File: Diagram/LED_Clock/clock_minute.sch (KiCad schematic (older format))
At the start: 34 parts, among them U3 MCP23017-E_SP

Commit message: updated
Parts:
- U3: symbol LED_Clock-rescue:MCP23017-E_SP-dk_Interface-I-O-Expanders -> Personal:MCP23017-Min
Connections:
- net at R8.2: now also U3.23 (GPA2); no longer U3.22 (GPA1)
- net at R9.2: now also U3.22 (GPA1); no longer U3.23 (GPA2)
- net at R14.2: now also U3.4 (GPB3); no longer U3.28 (GPA7)
- net at U3.21 (GPA0): now also R10.2; no longer R7.2
- net at U3.24 (GPA3): now also R7.2; no longer R10.2
- net at U3.25 (GPA4): now also R21.2; no longer R11.2
- net at U3.26 (GPA5): now also R20.2; no longer R12.2
- net at U3.27 (GPA6): now also R19.2; no longer R13.2
- net GPB0: no longer names the net of U3.1 (GPB0)
- net GPB0: now also R17.2; no longer R15.2
- net GPB1: no longer names the net of R16.2, U3.2 (GPB1)
- net GPB2: no longer names the net of U3.3 (GPB2)
- net GPB2: now also R15.2; no longer R17.2
- net GPB3: no longer names the net of R18.2
- net GPB3: now also U3.28 (GPA7); no longer U3.4 (GPB3)
- net GPB4: no longer names the net of U3.5 (GPB4)
- net GPB4: now also R13.2; no longer R19.2
- net GPB5: no longer names the net of U3.6 (GPB5)
- net GPB5: now also R12.2; no longer R20.2
- net GPB6: no longer names the net of U3.7 (GPB6)
- net GPB6: now also R11.2; no longer R21.2

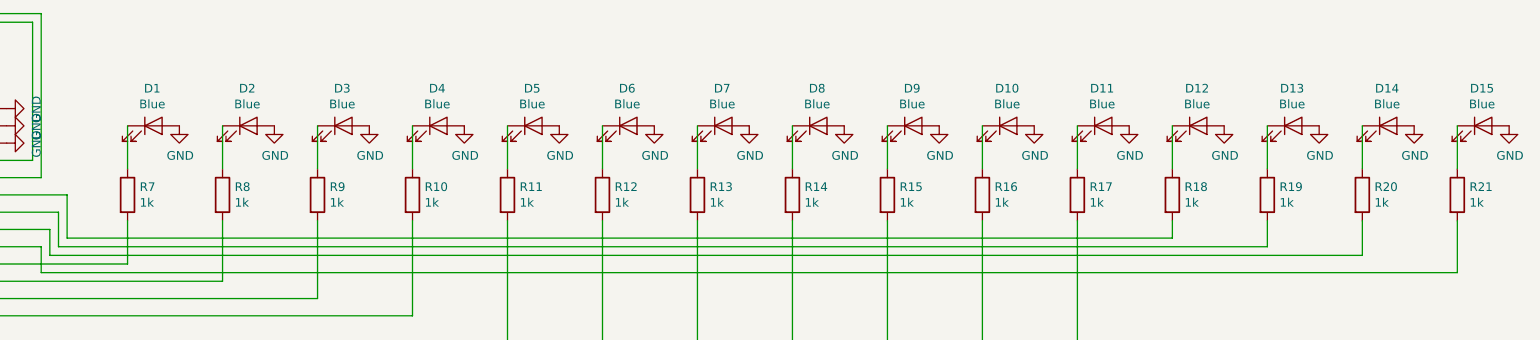
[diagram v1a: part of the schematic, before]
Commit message: Updated
led flipped the RTS symbol remade and JST4pin enlarged
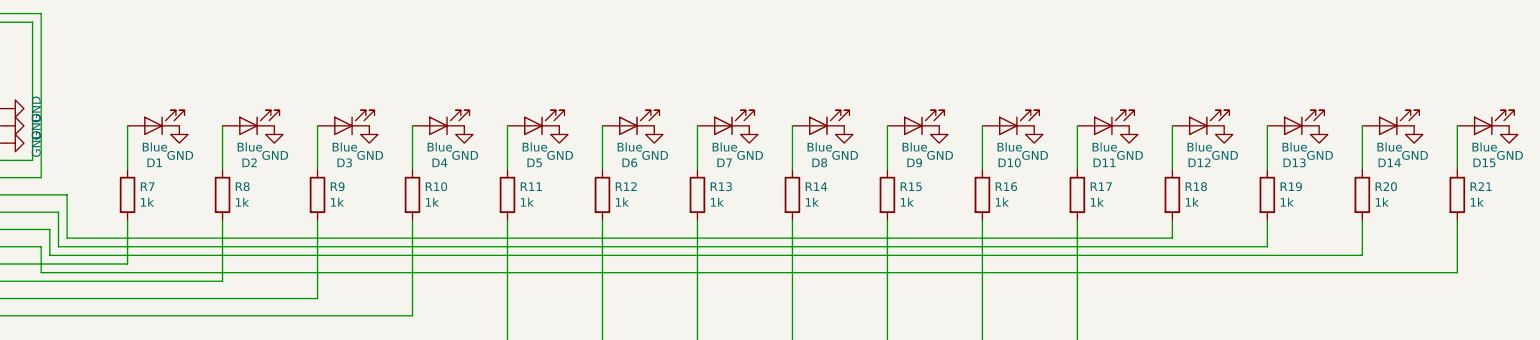
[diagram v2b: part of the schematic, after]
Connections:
- net GND: now also D1.1 (K), D10.1 (K), D11.1 (K), D12.1 (K), D13.1 (K), D14.1 (K), D15.1 (K), D2.1 (K), D3.1 (K), D4.1 (K), D5.1 (K), D6.1 (K), D7.1 (K), D8.1 (K), D9.1 (K); no longer D1.2 (A), D10.2 (A), D11.2 (A), D12.2 (A), D13.2 (A), D14.2 (A), D15.2 (A), D2.2 (A), D3.2 (A), D4.2 (A), D5.2 (A), D6.2 (A), D7.2 (A), D8.2 (A), D9.2 (A)
- net at R7.1: now also D1.2 (A); no longer D1.1 (K)
- net at R8.1: now also D2.2 (A); no longer D2.1 (K)
- net at R9.1: now also D3.2 (A); no longer D3.1 (K)
- net at R14.1: now also D8.2 (A); no longer D8.1 (K)
- net at R12.1: now also D6.2 (A); no longer D6.1 (K)
- net at R19.1: now also D13.2 (A); no longer D13.1 (K)
- net at R20.1: now also D14.2 (A); no longer D14.1 (K)
- net at R21.1: now also D15.2 (A); no longer D15.1 (K)
- net at R15.1: now also D9.2 (A); no longer D9.1 (K)
- net at R16.1: now also D10.2 (A); no longer D10.1 (K)
- net at R17.1: now also D11.2 (A); no longer D11.1 (K)
- net at R18.1: now also D12.2 (A); no longer D12.1 (K)
- net at R10.1: now also D4.2 (A); no longer D4.1 (K)
- net at R11.1: now also D5.2 (A); no longer D5.1 (K)
- net at R13.1: now also D7.2 (A); no longer D7.1 (K)
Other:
- moved on the sheet: D1, D10, D11, D12, D13, D14, D15, D2, D3, D4, D5, D6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
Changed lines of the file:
@@
 F 3 "~" H 3300 1450 50  0001 C CNN
 	1    3300 1450
-	1    0    0    -1
+	-1   0    0    1
 $EndComp
 $Comp
@@
 F 3 "~" H 3850 1450 50  0001 C CNN
 	1    3850 1450
-	1    0    0    -1
+	-1   0    0    1
 $EndComp
 $Comp
@@
 F 3 "~" H 4400 1450 50  0001 C CNN
 	1    4400 1450
-	1    0    0    -1
+	-1   0    0    1
 $EndComp
 $Comp
@@
 F 3 "~" H 4950 1450 50  0001 C CNN
 	1    4950 1450
-	1    0    0    -1
+	-1   0    0    1
 $EndComp
 $Comp
@@
 F 3 "~" H 5500 1450 50  0001 C CNN
 	1    5500 1450
-	1    0    0    -1
+	-1   0    0    1
 $EndComp
 $Comp
@@
 F 3 "~" H 6050 1450 50  0001 C CNN
 	1    6050 1450
-	1    0    0    -1
+	-1   0    0    1
 $EndComp
 $Comp
@@
 F 3 "~" H 6600 1450 50  0001 C CNN
 	1    6600 1450
-	1    0    0    -1
+	-1   0    0    1
 $EndComp
 $Comp
@@
 F 3 "~" H 7150 1450 50  0001 C CNN
 	1    7150 1450
-	1    0    0    -1
+	-1   0    0    1
 $EndComp
 $Comp
@@
 F 3 "~" H 7700 1450 50  0001 C CNN
 	1    7700 1450
-	1    0    0    -1
+	-1   0    0    1
 $EndComp
 $Comp
@@
 F 3 "~" H 8250 1450 50  0001 C CNN
 	1    8250 1450
-	1    0    0    -1
+	-1   0    0    1
 $EndComp
 $Comp
@@
 F 3 "~" H 8800 1450 50  0001 C CNN
 	1    8800 1450
-	1    0    0    -1
+	-1   0    0    1
 $EndComp
 $Comp
@@
 F 3 "~" H 9350 1450 50  0001 C CNN
 	1    9350 1450
-	1    0    0    -1
+	-1   0    0    1
 $EndComp
 $Comp
@@
 F 3 "~" H 9900 1450 50  0001 C CNN
 	1    9900 1450
-	1    0    0    -1
+	-1   0    0    1
 $EndComp
 $Comp
@@
 F 3 "~" H 10450 1450 50  0001 C CNN
 	1    10450 1450
-	1    0    0    -1
+	-1   0    0    1
 $EndComp
 $Comp
@@
 F 3 "~" H 11000 1450 50  0001 C CNN
 	1    11000 1450
-	1    0    0    -1
-$EndComp
-$Comp
+	-1   0    0    1
+$EndComp
+$Comp
